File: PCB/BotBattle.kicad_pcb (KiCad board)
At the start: 2 copper layers, 60.5 x 86 mm, 15 parts, among them J1 uit_Nema_17, J2 uit_Nema_17, J3 Conn_02x20_Odd_Even, J5 uit_buck_converter_raspberry_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, J6 Screw_Terminal_01x02, J7 ingang_lipo, U1 MCP3008-I/P

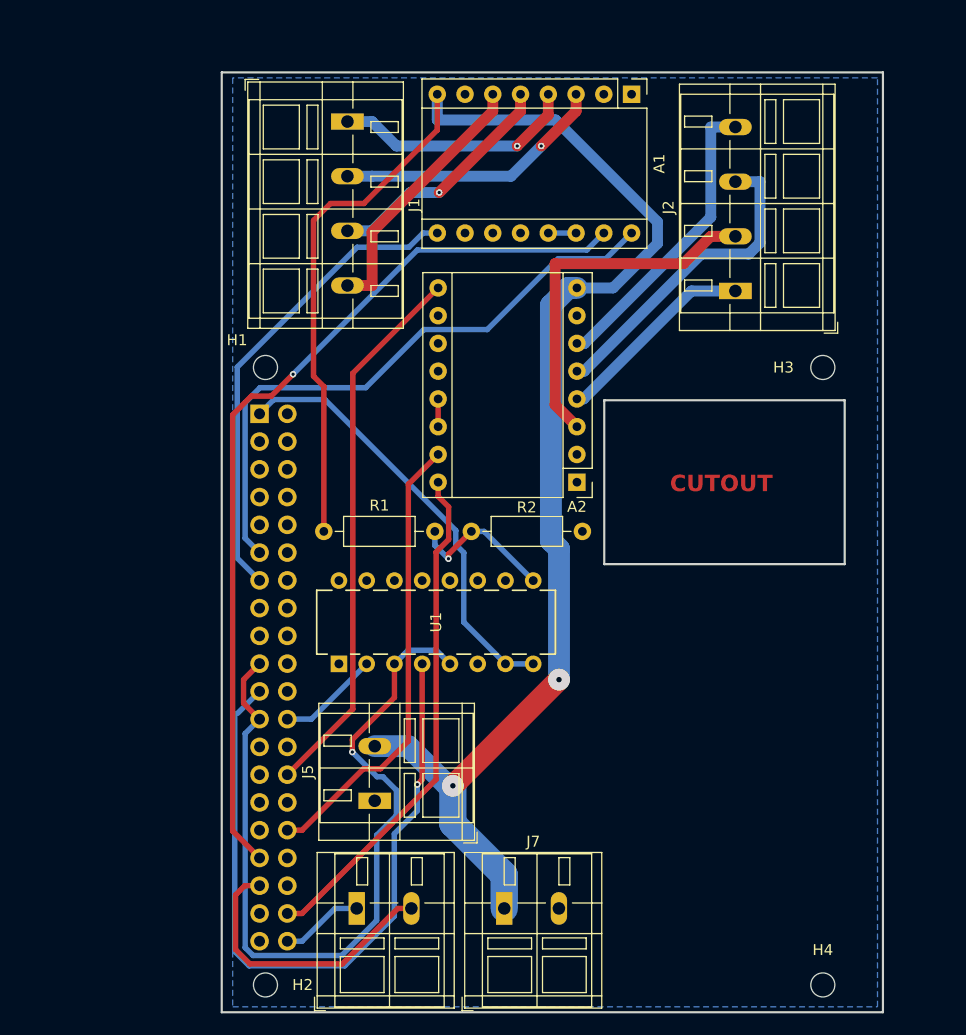
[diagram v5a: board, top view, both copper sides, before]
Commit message: Commit Type: Enhacement
Updated the pcb with fixes for DRV8825

Signed-off-by: ButrosGroot <butrosgroot@gmail.com>
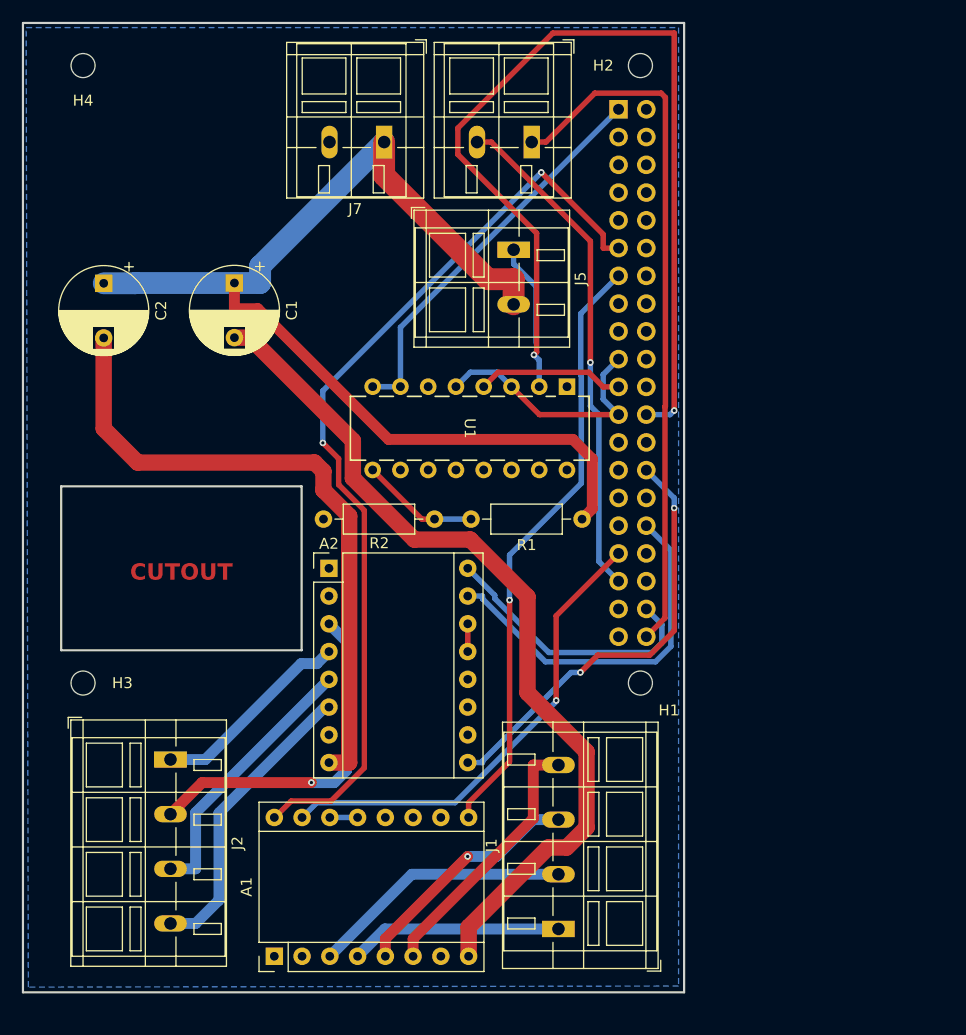
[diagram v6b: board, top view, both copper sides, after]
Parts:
- added C1: C, Capacitor_THT:CP_Radial_D8.0mm_P5.00mm, F.Cu at (147.2, 71.8)
- added C2: C, Capacitor_THT:CP_Radial_D8.0mm_P5.00mm, F.Cu at (135.2, 71.8)
- J5: value uit_buck_converter_raspberry_pi -> uit_buck_converter
- J6: value Screw_Terminal_01x02 -> Uitgang Wapen
- moved H4 108.0 mm to (133.3, 51.9), turned to 180 degrees
- moved H2 90.9 mm to (184.3, 51.9), turned to 180 degrees
- moved A1 85.4 mm to (150.8, 133.4), turned to 90 degrees
- moved J1 76.4 mm to (176.8, 130.9), turned to 90 degrees
- moved H3 73.6 mm to (133.3, 108.4), turned to 180 degrees
- moved J6 71.9 mm to (174.4, 58.9), turned to 180 degrees
- moved J7 71.0 mm to (160.9, 58.9), turned to 180 degrees
- moved J2 67.2 mm to (141.3, 115.4), turned to -90 degrees
- moved J5 52.0 mm to (172.7, 68.7), turned to -90 degrees
- moved H1 44.8 mm to (184.3, 108.4), turned to 180 degrees
- moved J3 43.1 mm to (182.3, 55.9)
- moved U1 32.8 mm to (177.6, 81.3), turned to -90 degrees
- moved A2 24.0 mm to (155.8, 97.9), turned to 0 degrees
- moved R1 23.7 mm to (179.0, 93.4), turned to 180 degrees
- moved R2 3.55 mm to (165.5, 93.4), turned to 180 degrees
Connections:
- A1 pad 7: unconnected-(A1-GND-Pad7) -> GND
- A2 pad 7: unconnected-(A2-GND-Pad7) -> GND
- A2 pad 8: Net-(A1-VMOT) -> Net-(A2-VMOT)
- J5 pad 2: Net-(A1-VMOT) -> Net-(J5-Pin_2)
- J7 pad 1: Net-(A1-VMOT) -> Net-(J5-Pin_2)
- R1 pad 1: Net-(A1-VMOT) -> Net-(J5-Pin_2)
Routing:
- net Net-(J5-Pin_2): track 0.00 -> 99.7 mm
- net Net-(A1-VMOT): track 157.7 -> 79.2 mm, vias 2 -> 0
- net Net-(J3-Pin_24): track 9.36 -> 87.6 mm, vias 0 -> 2
- net Net-(A2-VMOT): track 0.00 -> 59.5 mm
- net Net-(J3-Pin_40): track 7.59 -> 64.3 mm
- net Net-(J3-Pin_21): track 65.8 -> 13.4 mm, vias 1 -> 0
- net Net-(J3-Pin_19): track 75.3 -> 23.3 mm, vias 1 -> 0
- net Net-(A1-STEP): track 82.4 -> 43.6 mm
- net Net-(A1-DIR): track 56.1 -> 85.1 mm, vias 0 -> 2
- net Net-(A2-DIR): track 46.8 -> 25.2 mm
- net Net-(J3-Pin_35): track 26.3 -> 46.3 mm, vias 0 -> 1
- net Net-(A1-~{EN}): track 43.7 -> 55.3 mm, vias 0 -> 1
- net Net-(A2-~{EN}): track 50.3 -> 39.7 mm, vias 0 -> 2
- net GND: track 0.00 -> 9.39 mm
- net Net-(A2-STEP): track 41.8 -> 33.8 mm
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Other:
- board size 60.5 x 86 mm -> 60.5 x 88.7 mm

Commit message: Commit Type: Update
Final pcb design

Signed-off-by: ButrosGroot <butrosgroot@gmail.com>
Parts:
- J5: value uit_buck_converter -> uit_buck_converter_raspberry_pi
- J6: value Uitgang Wapen -> Screw_Terminal_01x02
- moved C2 38.2 mm to (173.3, 74.4), turned to 90 degrees
- moved J5 28.2 mm to (146.5, 58.2), turned to 180 degrees
- moved C1 16.8 mm to (163.8, 74.4), turned to 90 degrees
- moved J7 14.0 mm to (174.8, 58.3)
- moved J6 13.6 mm to (160.8, 58.3)
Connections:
- A2 pad 8: Net-(A2-VMOT) -> Net-(A1-VMOT)
- C1 pad 1: Net-(J5-Pin_2) -> Net-(A1-VMOT)
- C1 pad 2: Net-(A1-VMOT) -> GND
- C2 pad 1: Net-(J5-Pin_2) -> Net-(A1-VMOT)
- C2 pad 2: Net-(A2-VMOT) -> GND
- J3 pad 23: Net-(J3-Pin_19) -> Net-(J3-Pin_23)
- J5 pad 2: Net-(J5-Pin_2) -> Net-(A1-VMOT)
- J7 pad 1: Net-(J5-Pin_2) -> Net-(A1-VMOT)
- R1 pad 1: Net-(J5-Pin_2) -> Net-(A1-VMOT)
- U1 pad 1: GND -> Net-(R1-Pad2)
- U1 pad 10: unconnected-(U1-Pad10) -> Net-(J3-Pin_24)
- U1 pad 11: unconnected-(U1-Pad11) -> Net-(J3-Pin_19)
- U1 pad 12: unconnected-(U1-Pad12) -> Net-(J3-Pin_21)
- U1 pad 13: unconnected-(U1-Pad13) -> Net-(J3-Pin_23)
- U1 pad 14: unconnected-(U1-Pad14) -> GND
- U1 pad 15: unconnected-(U1-Pad15) -> Net-(J3-3v3_power)
- U1 pad 16: unconnected-(U1-Pad16) -> Net-(J3-3v3_power)
- U1 pad 2: Net-(J3-Pin_24) -> unconnected-(U1-Pad2)
- U1 pad 3: Net-(J3-Pin_19) -> unconnected-(U1-Pad3)
- U1 pad 4: Net-(J3-Pin_21) -> unconnected-(U1-Pad4)
- U1 pad 5: Net-(J3-Pin_19) -> unconnected-(U1-Pad5)
- U1 pad 6: GND -> unconnected-(U1-Pad6)
- U1 pad 7: Net-(J3-3v3_power) -> unconnected-(U1-Pad7)
- U1 pad 8: Net-(J3-3v3_power) -> unconnected-(U1-Pad8)
- U1 pad 9: Net-(R1-Pad2) -> GND
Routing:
- net Net-(A1-VMOT): track 79.2 -> 201.9 mm, vias 0 -> 3
- net Net-(J5-Pin_2): track 99.7 -> 0.00 mm
- net Net-(A2-VMOT): track 59.5 -> 0.00 mm
- net Net-(R1-Pad2): track 10.9 -> 38.7 mm, vias 0 -> 1
- net Net-(J3-Pin_35): track 46.3 -> 63.0 mm
- net Net-(J3-Pin_24): track 87.6 -> 71.4 mm
- net Net-(J3-Pin_23): track 0.00 -> 14.4 mm, vias 0 -> 1
- net GND: track 9.39 -> 0.65 mm
- net Net-(A1-DIR): track 85.1 -> 77.0 mm
- net Net-(A2-B1): track 24.7 -> 32.1 mm
- net Net-(A2-DIR): track 25.2 -> 31.6 mm
- net Net-(J3-Pin_21): track 13.4 -> 19.1 mm, vias 0 -> 1
- net Net-(A2-~{EN}): track 39.7 -> 43.6 mm, vias 2 -> 0
- net Net-(A1-A2): track 24.0 -> 27.6 mm
- net Net-(J3-Pin_40): track 64.3 -> 61.2 mm
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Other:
- board size 60.5 x 88.7 mm -> 60.3 x 88.1 mm
